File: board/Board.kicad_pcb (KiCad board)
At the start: 2 copper layers, 62 parts, among them J1 GS3, J10 CONN_01X03, J11 CONN_01X03, J12 GS3, J13 GS3, J14 CONN_01X02, J15 CONN_01X03, J16 GS2, J17 CONN_01X01, J2 CONN_02X04, J3 CONN_01X03, J4 CONN_01X03, J5 CONN_01X03, J6 CONN_01X03, J7 CONN_01X03, J8 CONN_01X03, J9 CONN_01X03, SW1 SW_Push, U1 STM32F410RBTx, U2 SN74LVC1G04, U3 LF33ABDT-TR, U4 ICM-20689, U5 MAG3110, U6 MS5637, Y1 25 MHz

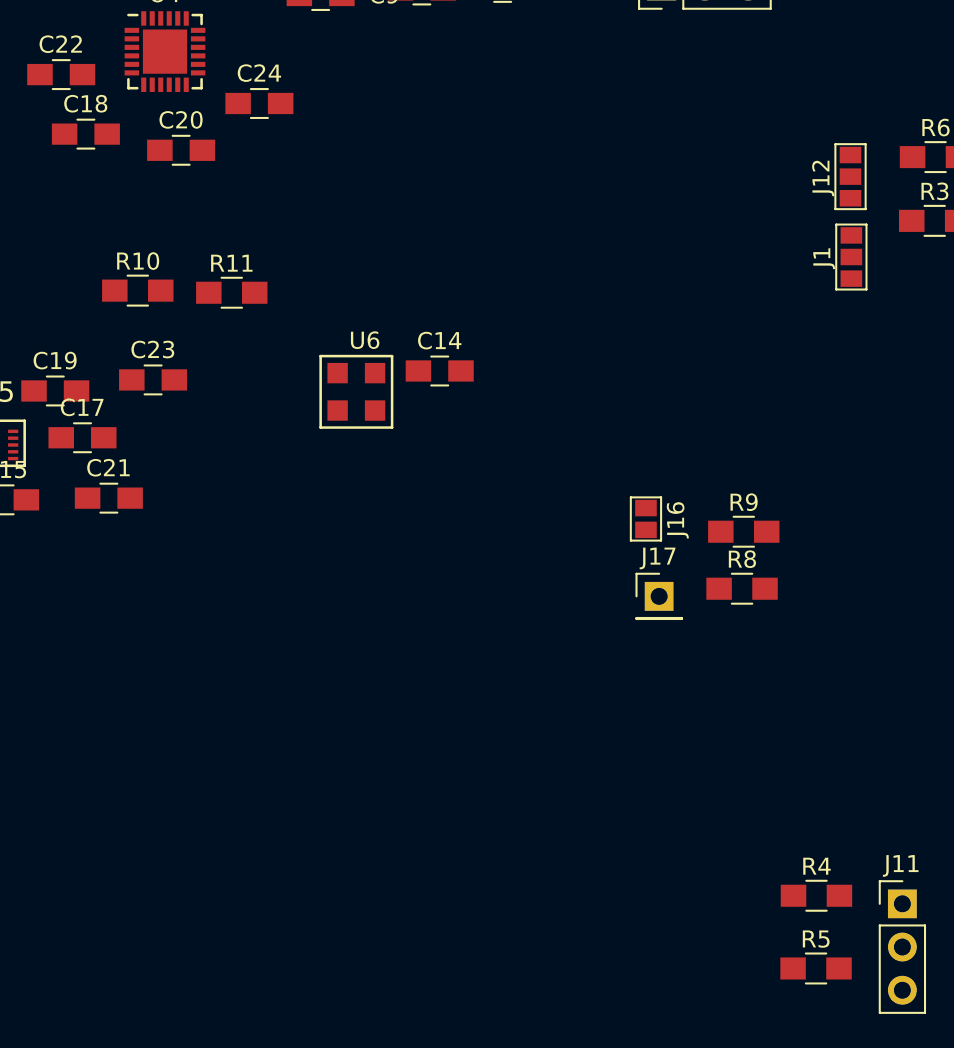
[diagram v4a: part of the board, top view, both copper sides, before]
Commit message: using resistor array for I2C pullups
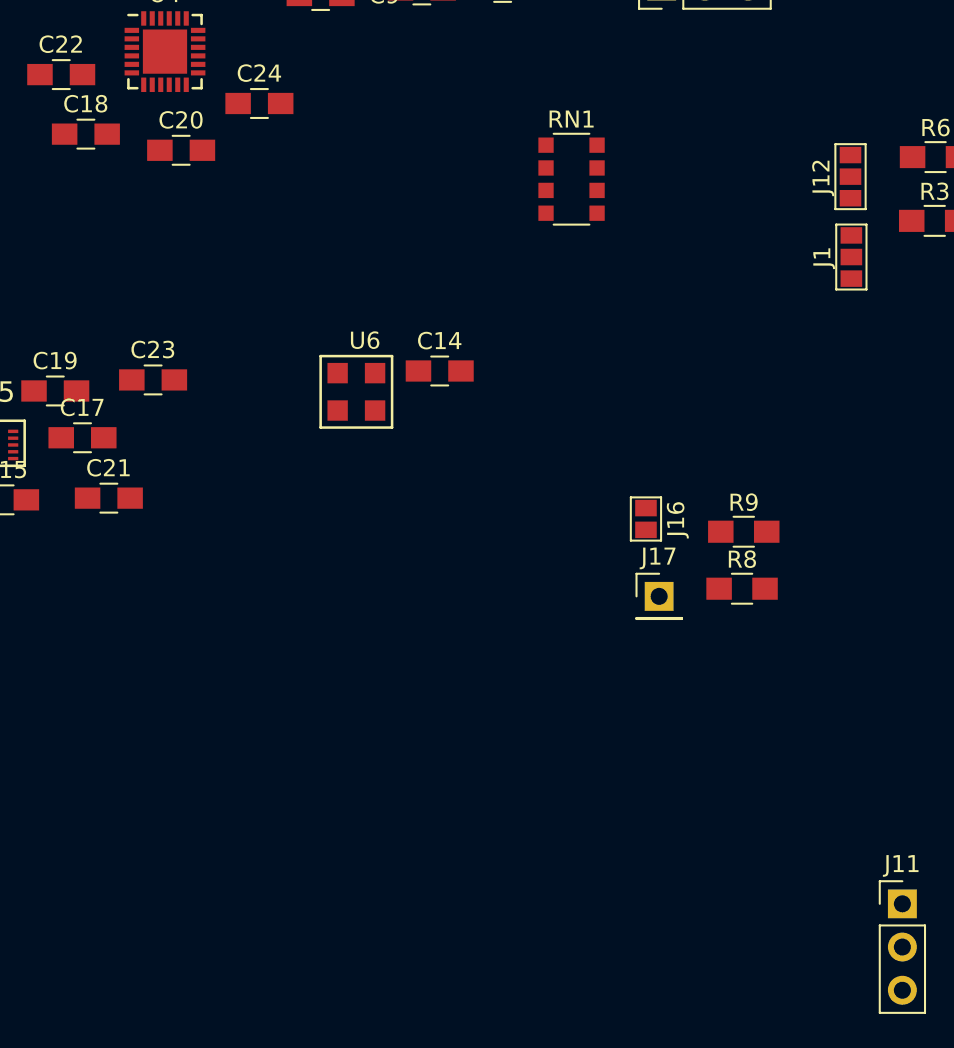
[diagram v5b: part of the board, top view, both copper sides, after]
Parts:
- removed R10, R11, R4, R5: 10K, Resistors_SMD:R_0805_HandSoldering
- added RN1: 4.7K, Resistors_SMD:R_Array_Convex_4x1206, F.Cu at (141.3, 115.2)
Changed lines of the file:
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@@
     (links 151)
     (no_connects 151)
-    (area 95.614286 62.095 212.358334 166.235)
+    (area 0 0 0 0)
     (thickness 1.6)
     (drawings 0)
     (tracks 0)
     (zones 0)
-    (modules 62)
+    (modules 59)
     (nets 76)
   )
@@
   )
   (module Resistors_SMD:R_0805_HandSoldering (layer F.Cu)
-    (at 155.75 157.275)
-    (descr "Resistor SMD 0805, hand soldering")
-    (tags "resistor 0805")
-    (attr smd)
-    (fp_text reference R4 (at 0 -1.7) (layer F.SilkS)
-      (effects (font (size 1 1) (thickness 0.15)))
-    )
-    (fp_text value 10K (at 0 1.75) (layer F.Fab)
-      (effects (font (size 1 1) (thickness 0.15)))
-    )
-    (fp_text user %R (at 0 0) (layer F.Fab)
-      (effects (font (size 0.5 0.5) (thickness 0.075)))
-    )
-    (fp_line (start -1 0.62) (end -1 -0.62) (layer F.Fab) (width 0.1))
-    (fp_line (start 1 0.62) (end -1 0.62) (layer F.Fab) (width 0.1))
-    (fp_line (start 1 -0.62) (end 1 0.62) (layer F.Fab) (width 0.1))
-    (fp_line (start -1 -0.62) (end 1 -0.62) (layer F.Fab) (width 0.1))
-    (fp_line (start 0.6 0.88) (end -0.6 0.88) (layer F.SilkS) (width 0.12))
-    (fp_line (start -0.6 -0.88) (end 0.6 -0.88) (layer F.SilkS) (width 0.12))
-    (fp_line (start -2.35 -0.9) (end 2.35 -0.9) (layer F.CrtYd) (width 0.05))
-    (fp_line (start -2.35 -0.9) (end -2.35 0.9) (layer F.CrtYd) (width 0.05))
-    (fp_line (start 2.35 0.9) (end 2.35 -0.9) (layer F.CrtYd) (width 0.05))
-    (fp_line (start 2.35 0.9) (end -2.35 0.9) (layer F.CrtYd) (width 0.05))
-    (pad 1 smd rect (at -1.35 0) (size 1.5 1.3) (layers F.Cu F.Paste F.Mask)
-      (net 5 VCC))
-    (pad 2 smd rect (at 1.35 0) (size 1.5 1.3) (layers F.Cu F.Paste F.Mask)
-      (net 72 I2C1_SCL))
-    (model ${KISYS3DMOD}/Resistors_SMD.3dshapes/R_0805.wrl
-      (at (xyz 0 0 0))
-      (scale (xyz 1 1 1))
-      (rotate (xyz 0 0 0))
-    )
-  )
-  (module Resistors_SMD:R_0805_HandSoldering (layer F.Cu)
-    (at 155.725 161.55)
-    (descr "Resistor SMD 0805, hand soldering")
-    (tags "resistor 0805")
-    (attr smd)
-    (fp_text reference R5 (at 0 -1.7) (layer F.SilkS)
-      (effects (font (size 1 1) (thickness 0.15)))
-    )
-    (fp_text value 10K (at 0 1.75) (layer F.Fab)
-      (effects (font (size 1 1) (thickness 0.15)))
-    )
-    (fp_text user %R (at 0 0) (layer F.Fab)
-      (effects (font (size 0.5 0.5) (thickness 0.075)))
-    )
-    (fp_line (start -1 0.62) (end -1 -0.62) (layer F.Fab) (width 0.1))
-    (fp_line (start 1 0.62) (end -1 0.62) (layer F.Fab) (width 0.1))
-    (fp_line (start 1 -0.62) (end 1 0.62) (layer F.Fab) (width 0.1))
-    (fp_line (start -1 -0.62) (end 1 -0.62) (layer F.Fab) (width 0.1))
-    (fp_line (start 0.6 0.88) (end -0.6 0.88) (layer F.SilkS) (width 0.12))
-    (fp_line (start -0.6 -0.88) (end 0.6 -0.88) (layer F.SilkS) (width 0.12))
-    (fp_line (start -2.35 -0.9) (end 2.35 -0.9) (layer F.CrtYd) (width 0.05))
-    (fp_line (start -2.35 -0.9) (end -2.35 0.9) (layer F.CrtYd) (width 0.05))
-    (fp_line (start 2.35 0.9) (end 2.35 -0.9) (layer F.CrtYd) (width 0.05))
-    (fp_line (start 2.35 0.9) (end -2.35 0.9) (layer F.CrtYd) (width 0.05))
-    (pad 1 smd rect (at -1.35 0) (size 1.5 1.3) (layers F.Cu F.Paste F.Mask)
-      (net 5 VCC))
-    (pad 2 smd rect (at 1.35 0) (size 1.5 1.3) (layers F.Cu F.Paste F.Mask)
-      (net 73 I2C1_SDA))
-    (model ${KISYS3DMOD}/Resistors_SMD.3dshapes/R_0805.wrl
-      (at (xyz 0 0 0))
-      (scale (xyz 1 1 1))
-      (rotate (xyz 0 0 0))
-    )
-  )
-  (module Resistors_SMD:R_0805_HandSoldering (layer F.Cu)
     (at 162.75 113.85)
     (descr "Resistor SMD 0805, hand soldering")
@@
     )
   )
-  (module Resistors_SMD:R_0805_HandSoldering (layer F.Cu)
-    (at 115.85 121.7)
-    (descr "Resistor SMD 0805, hand soldering")
-    (tags "resistor 0805")
-    (attr smd)
-    (fp_text reference R10 (at 0 -1.7) (layer F.SilkS)
-      (effects (font (size 1 1) (thickness 0.15)))
-    )
-    (fp_text value 10K (at 0 1.75) (layer F.Fab)
-      (effects (font (size 1 1) (thickness 0.15)))
-    )
-    (fp_text user %R (at 0 0) (layer F.Fab)
-      (effects (font (size 0.5 0.5) (thickness 0.075)))
-    )
-    (fp_line (start -1 0.62) (end -1 -0.62) (layer F.Fab) (width 0.1))
-    (fp_line (start 1 0.62) (end -1 0.62) (layer F.Fab) (width 0.1))
-    (fp_line (start 1 -0.62) (end 1 0.62) (layer F.Fab) (width 0.1))
-    (fp_line (start -1 -0.62) (end 1 -0.62) (layer F.Fab) (width 0.1))
-    (fp_line (start 0.6 0.88) (end -0.6 0.88) (layer F.SilkS) (width 0.12))
-    (fp_line (start -0.6 -0.88) (end 0.6 -0.88) (layer F.SilkS) (width 0.12))
-    (fp_line (start -2.35 -0.9) (end 2.35 -0.9) (layer F.CrtYd) (width 0.05))
-    (fp_line (start -2.35 -0.9) (end -2.35 0.9) (layer F.CrtYd) (width 0.05))
-    (fp_line (start 2.35 0.9) (end 2.35 -0.9) (layer F.CrtYd) (width 0.05))
-    (fp_line (start 2.35 0.9) (end -2.35 0.9) (layer F.CrtYd) (width 0.05))
-    (pad 1 smd rect (at -1.35 0) (size 1.5 1.3) (layers F.Cu F.Paste F.Mask)
-      (net 5 VCC))
-    (pad 2 smd rect (at 1.35 0) (size 1.5 1.3) (layers F.Cu F.Paste F.Mask)
+  (module Resistors_SMD:R_Array_Convex_4x1206 (layer F.Cu)
+    (at 141.35 115.15)
+    (descr "Chip Resistor Network, ROHM MNR34 (see mnr_g.pdf)")
+    (tags "resistor array")
+    (attr smd)
+    (fp_text reference RN1 (at 0 -3.5) (layer F.SilkS)
+      (effects (font (size 1 1) (thickness 0.15)))
+    )
+    (fp_text value 4.7K (at 0 3.5) (layer F.Fab)
+      (effects (font (size 1 1) (thickness 0.15)))
+    )
+    (fp_text user %R (at 0 0 90) (layer F.Fab)
+      (effects (font (size 0.7 0.7) (thickness 0.105)))
+    )
+    (fp_line (start -1.6 -2.6) (end -1.6 2.6) (layer F.Fab) (width 0.1))
+    (fp_line (start -1.6 2.6) (end 1.6 2.6) (layer F.Fab) (width 0.1))
+    (fp_line (start 1.6 2.6) (end 1.6 -2.6) (layer F.Fab) (width 0.1))
+    (fp_line (start 1.6 -2.6) (end -1.6 -2.6) (layer F.Fab) (width 0.1))
+    (fp_line (start 1.05 2.67) (end -1.05 2.67) (layer F.SilkS) (width 0.12))
+    (fp_line (start 1.05 -2.67) (end -1.05 -2.67) (layer F.SilkS) (width 0.12))
+    (fp_line (start -2.21 -2.85) (end 2.2 -2.85) (layer F.CrtYd) (width 0.05))
+    (fp_line (start -2.21 -2.85) (end -2.21 2.85) (layer F.CrtYd) (width 0.05))
+    (fp_line (start 2.2 2.85) (end 2.2 -2.85) (layer F.CrtYd) (width 0.05))
+    (fp_line (start 2.2 2.85) (end -2.21 2.85) (layer F.CrtYd) (width 0.05))
+    (pad 1 smd rect (at -1.5 -2) (size 0.9 0.9) (layers F.Cu F.Paste F.Mask)
+      (net 73 I2C1_SDA))
+    (pad 4 smd rect (at -1.5 2) (size 0.9 0.9) (layers F.Cu F.Paste F.Mask)
+      (net 74 I2C2_SCL))
+    (pad 2 smd rect (at -1.5 -0.66) (size 0.9 0.9) (layers F.Cu F.Paste F.Mask)
+      (net 72 I2C1_SCL))
+    (pad 3 smd rect (at -1.5 0.66) (size 0.9 0.9) (layers F.Cu F.Paste F.Mask)
       (net 75 I2C2_SDA))
-    (model ${KISYS3DMOD}/Resistors_SMD.3dshapes/R_0805.wrl
-      (at (xyz 0 0 0))
-      (scale (xyz 1 1 1))
-      (rotate (xyz 0 0 0))
-    )
-  )
-  (module Resistors_SMD:R_0805_HandSoldering (layer F.Cu)
-    (at 121.375 121.825)
-    (descr "Resistor SMD 0805, hand soldering")
-    (tags "resistor 0805")
-    (attr smd)
-    (fp_text reference R11 (at 0 -1.7) (layer F.SilkS)
-      (effects (font (size 1 1) (thickness 0.15)))
-    )
-    (fp_text value 10K (at 0 1.75) (layer F.Fab)
-      (effects (font (size 1 1) (thickness 0.15)))
-    )
-    (fp_text user %R (at 0 0) (layer F.Fab)
-      (effects (font (size 0.5 0.5) (thickness 0.075)))
-    )
-    (fp_line (start -1 0.62) (end -1 -0.62) (layer F.Fab) (width 0.1))
-    (fp_line (start 1 0.62) (end -1 0.62) (layer F.Fab) (width 0.1))
-    (fp_line (start 1 -0.62) (end 1 0.62) (layer F.Fab) (width 0.1))
-    (fp_line (start -1 -0.62) (end 1 -0.62) (layer F.Fab) (width 0.1))
-    (fp_line (start 0.6 0.88) (end -0.6 0.88) (layer F.SilkS) (width 0.12))
-    (fp_line (start -0.6 -0.88) (end 0.6 -0.88) (layer F.SilkS) (width 0.12))
-    (fp_line (start -2.35 -0.9) (end 2.35 -0.9) (layer F.CrtYd) (width 0.05))
-    (fp_line (start -2.35 -0.9) (end -2.35 0.9) (layer F.CrtYd) (width 0.05))
-    (fp_line (start 2.35 0.9) (end 2.35 -0.9) (layer F.CrtYd) (width 0.05))
-    (fp_line (start 2.35 0.9) (end -2.35 0.9) (layer F.CrtYd) (width 0.05))
-    (pad 1 smd rect (at -1.35 0) (size 1.5 1.3) (layers F.Cu F.Paste F.Mask)
-      (net 5 VCC))
-    (pad 2 smd rect (at 1.35 0) (size 1.5 1.3) (layers F.Cu F.Paste F.Mask)
-      (net 74 I2C2_SCL))
-    (model ${KISYS3DMOD}/Resistors_SMD.3dshapes/R_0805.wrl
-      (at (xyz 0 0 0))
-      (scale (xyz 1 1 1))
+    (pad 7 smd rect (at 1.5 -0.66) (size 0.9 0.9) (layers F.Cu F.Paste F.Mask)
+      (net 5 VCC))
+    (pad 8 smd rect (at 1.5 -2) (size 0.9 0.9) (layers F.Cu F.Paste F.Mask)
+      (net 5 VCC))
+    (pad 5 smd rect (at 1.5 2) (size 0.9 0.9) (layers F.Cu F.Paste F.Mask)
+      (net 5 VCC))
+    (pad 6 smd rect (at 1.5 0.66) (size 0.9 0.9) (layers F.Cu F.Paste F.Mask)
+      (net 5 VCC))
+    (model ${KISYS3DMOD}/Resistors_SMD.3dshapes/R_Array_Convex_4x1206.wrl
+      (at (xyz 0 0 0))
+      (scale (xyz 1 1 1))

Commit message: put everything togheter
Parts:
- moved SW1 79.1 mm to (105.7, 118.3)
- moved C3 79.1 mm to (106.2, 115.3)
- moved J15 70.0 mm to (150.9, 108.1)
- moved J13 61.6 mm to (151.3, 118.0)
- moved R8 61.5 mm to (106.5, 97.0)
- moved J17 60.9 mm to (106.0, 94.2)
- moved U2 60.6 mm to (146.9, 118.7)
- moved J16 60.1 mm to (105.3, 90.7)
- moved R9 58.1 mm to (106.5, 99.1), turned to 180 degrees
- moved R6 55.6 mm to (108.2, 103.2), turned to 180 degrees
- moved R3 55.3 mm to (108.2, 108.2)
- moved J11 51.6 mm to (146.7, 108.1)
- moved J12 50.6 mm to (108.0, 105.7), turned to 270 degrees
- moved J1 50.6 mm to (108.0, 110.7), turned to 270 degrees
- moved C19 32.4 mm to (141.9, 117.8), turned to 90 degrees
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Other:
- board outline added: 50.8 x 56.3 mm
